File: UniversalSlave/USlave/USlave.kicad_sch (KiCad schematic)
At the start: 18 parts, among them J1 Pluck EADG 1, J2 ISCP, J3 Power In, J4 I2C Test Point, J5 Pluck EADG 2, J6 Mute EADG, J7 I2C Through, J8 I2C In, SW1 SW_Push, U1 PIC16F1788

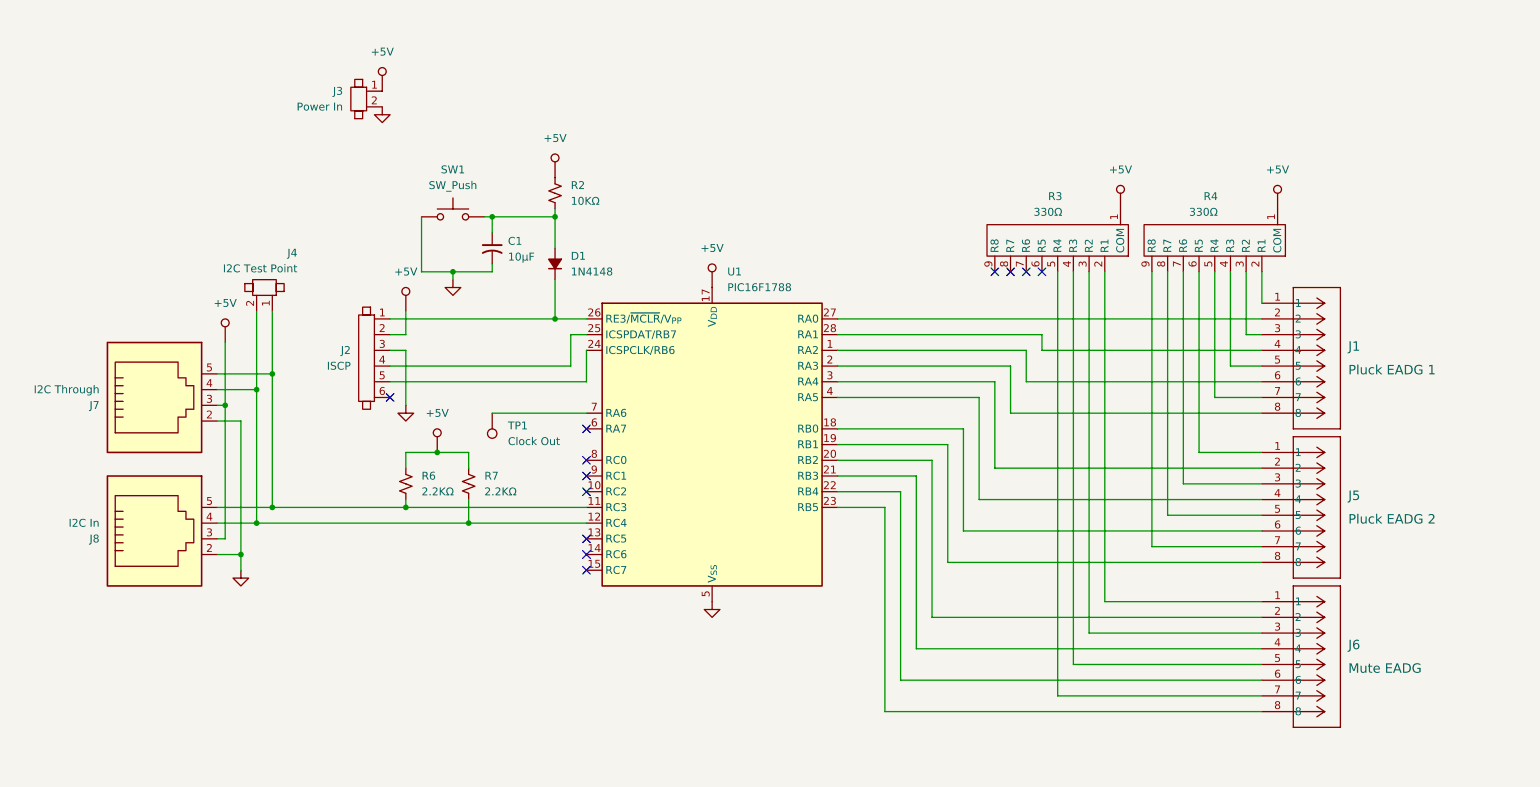
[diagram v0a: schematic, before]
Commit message: decided on utilizing a universal setup for the slave board
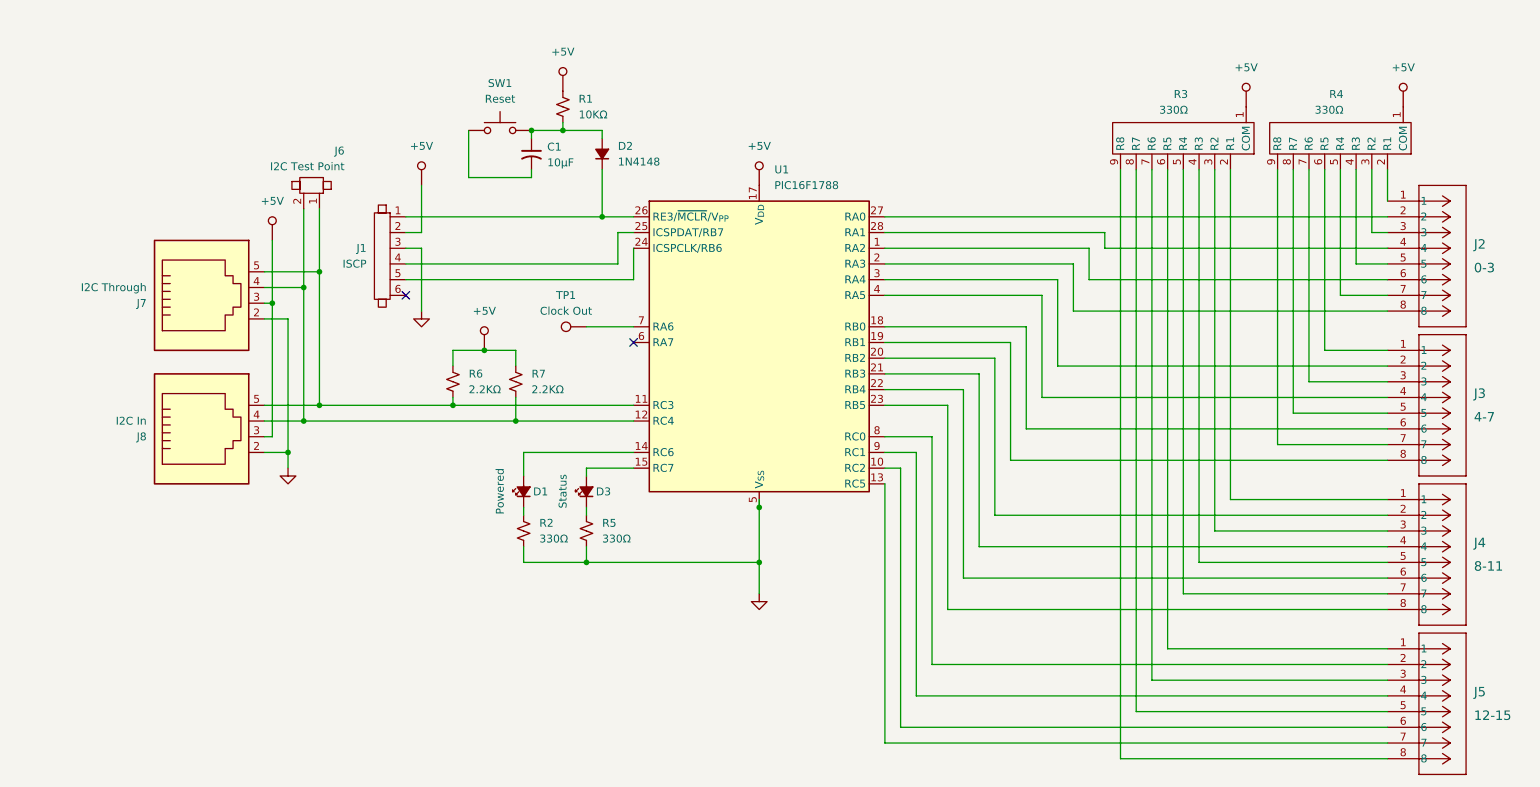
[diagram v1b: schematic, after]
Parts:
- removed D1: 1N4148, symbol Device:D_Small_Filled
- removed J1: Pluck EADG 1, CONN_SD-43045-004_08_MOL, symbol 2_JB_Custom_sym:8PinMolexConn
- removed J2: ISCP, symbol 2_JB_Custom_sym:Jumper_6_Pin
- removed J3: Power In, 2JB_Footprints:1X2_100mil_Header, symbol 2_JB_Custom_sym:Jumper_2_Pin
- removed J4: I2C Test Point, 2JB_Footprints:1X2_100mil_Header, symbol 2_JB_Custom_sym:Jumper_2_Pin
- removed J6: Mute EADG, CONN_SD-43045-004_08_MOL, symbol 2_JB_Custom_sym:8PinMolexConn
- added D1: Powered, symbol Device:LED_Small_Filled
- added D2: 1N4148, symbol Device:D_Small_Filled
- added D3: Status, symbol Device:LED_Small_Filled
- added J1: ISCP, symbol 2_JB_Custom_sym:Jumper_6_Pin
- added J2: 0-3, CONN_SD-43045-004_08_MOL, symbol 2_JB_Custom_sym:8PinMolexConn
- added J3: 4-7, CONN_SD-43045-004_08_MOL, symbol 2_JB_Custom_sym:8PinMolexConn
- added J4: 8-11, CONN_SD-43045-004_08_MOL, symbol 2_JB_Custom_sym:8PinMolexConn
- added J6: I2C Test Point, 2JB_Footprints:1X2_100mil_Header, symbol 2_JB_Custom_sym:Jumper_2_Pin
- added R1: 10KΩ, symbol Device:R_Small_US
- added R5: 330Ω, symbol Device:R_Small_US
- J5: value Pluck EADG 2 -> 12-15
- R2: value 10KΩ -> 330Ω
- SW1: value SW_Push -> Reset
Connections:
- net GND: now also R2.2, J1.3, R5.2; no longer C1.2, SW1.1
- net at C1.1, SW1.2: now also D2.2 (A), R1.2; no longer R2.2
- net at R4.6 (R5): now also J3.1; no longer J5.1
- net at J5.2: now also U1.8 (RC0); no longer U1.3 (RA4)
- net at R4.7 (R6): now also J3.3; no longer J5.3
- net at J5.4: now also U1.9 (RC1); no longer U1.4 (RA5)
- net at R4.8 (R7): now also J3.5; no longer J5.5
- net at J5.6: now also U1.10 (RC2); no longer U1.18 (RB0)
- net at R4.9 (R8): now also J3.7; no longer J5.7
- net at J5.8: now also R3.9 (R8); no longer U1.19 (RB1)
- net at J7.4, J8.4, R7.2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: now also J6.2
- net at J7.5, J8.5, R6.2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: now also J6.1
- net at R4.2 (R1): now also J2.1
- net at U1.27 (RA0): now also J2.2
- net at R4.3 (R2): now also J2.3
- net at U1.28 (RA1): now also J2.4
- net at R4.4 (R3): now also J2.5
- net at U1.1 (RA2): now also J2.6
- net at R4.5 (R4): now also J2.7
- net at U1.2 (RA3): now also J2.8
- net at U1.26 (RE3/~{MCLR}/V_{PP}): now also D2.1 (K), J1.1
- net at U1.25 (ICSPDAT/RB7): now also J1.4
- net at U1.24 (ICSPCLK/RB6): now also J1.5
- net at R2.1: now also D1.1 (K)
- net at R3.2 (R1): now also J4.1
- net at R3.3 (R2): now also J4.3
- net at R3.4 (R3): now also J4.5
- net at R3.5 (R4): now also J4.7
- net at R3.6 (R5): now also J5.1
- net at R3.7 (R6): now also J5.3
- net at R3.8 (R7): now also J5.5
- net at U1.13 (RC5): now also J5.7
- net at U1.14 (RC6): now also D1.2 (A)
- net at U1.15 (RC7): now also D3.2 (A)
- net at U1.20 (RB2): now also J4.2
- net at U1.21 (RB3): now also J4.4
- net at U1.22 (RB4): now also J4.6
- net at U1.23 (RB5): now also J4.8
- new net: D3.1 (K), R5.1
- new net: C1.2, SW1.1
- new net: J3.6, U1.18 (RB0)
- new net: J3.8, U1.19 (RB1)
- new net: J3.2, U1.3 (RA4)
- new net: J3.4, U1.4 (RA5)
- no-connect marks 12 -> 2
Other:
- moved on the sheet: J7, J8, R3, R4, R6, R7, U1

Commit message: designed universal PCB
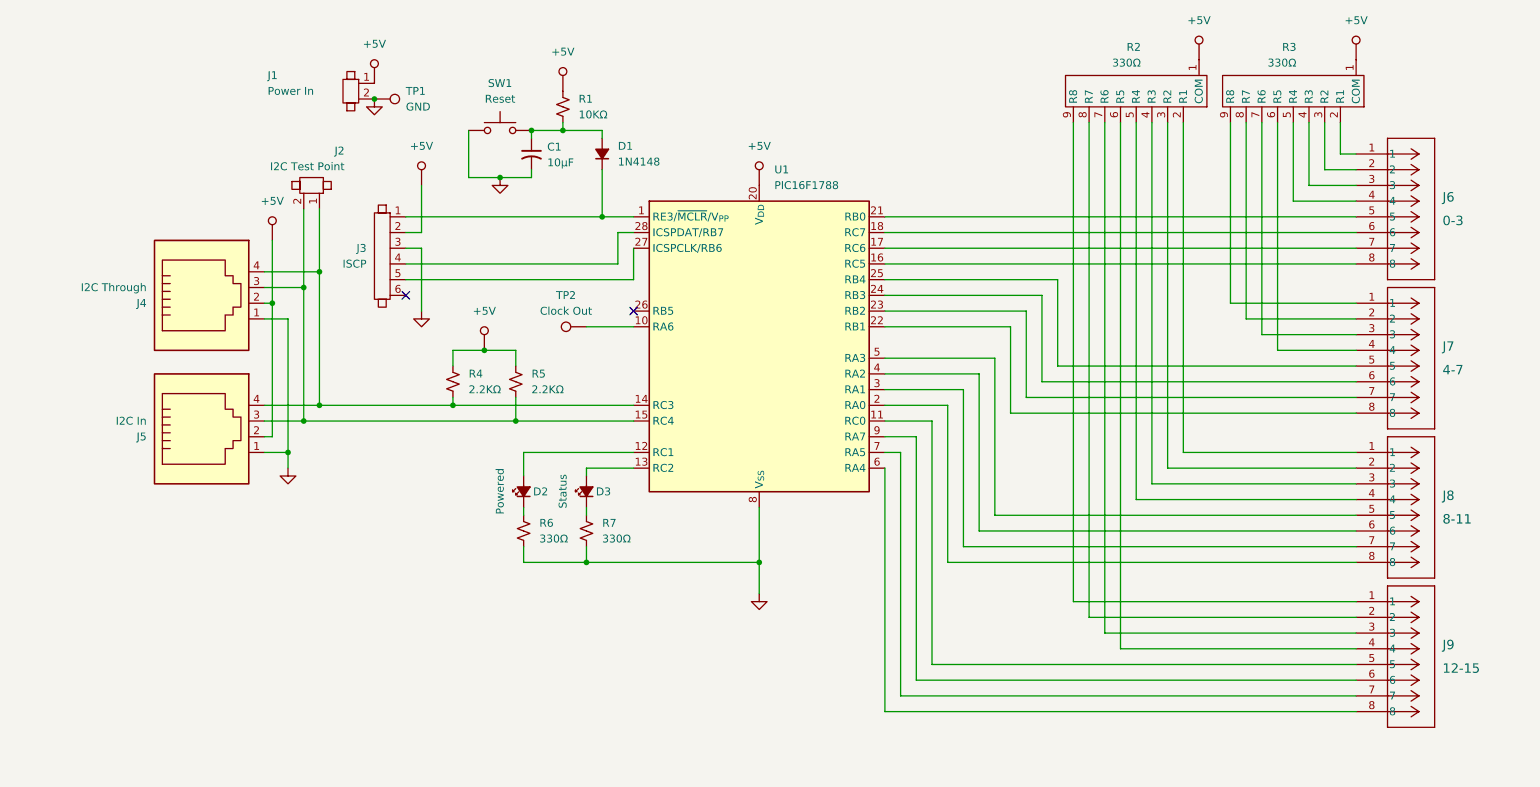
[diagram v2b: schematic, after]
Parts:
- removed J8: I2C In, 2JB_Footprints:RJ11, symbol Connector:RJ11
- added J1: Power In, 2JB_Footprints:2PinMolex, symbol 2_JB_Custom_sym:Jumper_2_Pin
- added J5: I2C In, 2JB_Footprints:RJ11, symbol Connector:RJ11
- added TP1: GND, 2JB_Footprints:1X1_100mil_Header, symbol Connector:TestPoint
- C1: footprint (none) -> Capacitor_THT:C_Radial_D6.3mm_H11.0mm_P2.50mm
- D1: renamed from D2; footprint (none) -> 2JB_Footprints:D_0805
- D2: renamed from D1; footprint (none) -> 2JB_Footprints:D_0805
- D3: footprint (none) -> 2JB_Footprints:D_0805
- J3: renamed from J1; footprint (none) -> 2JB_Footprints:1X6_100mil_Header
- J6: renamed from J2; footprint CONN_SD-43045-004_08_MOL -> 2JB_Footprints:8PinMolex_3.00mmPitch
- J7: renamed from J3; footprint CONN_SD-43045-004_08_MOL -> 2JB_Footprints:8PinMolex_3.00mmPitch
- J8: renamed from J4; footprint CONN_SD-43045-004_08_MOL -> 2JB_Footprints:8PinMolex_3.00mmPitch
- J9: renamed from J5; footprint CONN_SD-43045-004_08_MOL -> 2JB_Footprints:8PinMolex_3.00mmPitch
- R1: footprint (none) -> 2JB_Footprints:C_0805
- R2: renamed from R3; footprint (none) -> 2JB_Footprints:1x9_100mil_Header
- R3: renamed from R4; footprint (none) -> 2JB_Footprints:1x9_100mil_Header
- R6: renamed from R2; footprint (none) -> 2JB_Footprints:C_0805
- R7: renamed from R5; footprint (none) -> 2JB_Footprints:C_0805
- SW1: footprint (none) -> Button_Switch_THT:SW_TH_Tactile_Omron_B3F-100x
- TP2: renamed from TP1; footprint (none) -> 2JB_Footprints:1X1_100mil_Header
- renumbered J6 to J2, J7 to J4, R6 to R4, R7 to R5
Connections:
- net GND: now also C1.2, J4.1, SW1.1, U1.19 (V_{SS}), U1.8 (V_{SS}), J1.2, J5.1, TP1.1; no longer J4.2, U1.16 (V_{SS}), U1.5 (V_{SS})
- net at TP2.1: now also U1.10 (RA6); no longer U1.7 (RA6)
- net at D1.1 (K), J3.1: now also U1.1 (RE3/~{MCLR}/V_{PP}); no longer U1.26 (RE3/~{MCLR}/V_{PP})
- net at J4.3: now also J2.2, R5.2, U1.15 (RC4), J5.3
- net at J2.1, R4.2: now also J4.4, U1.14 (RC3), J5.4; no longer J4.5, U1.11 (RC3)
- net at R3.3 (R2): now also J6.2; no longer J6.3
- net at R3.4 (R3): now also J6.3; no longer J6.5
- net at R3.5 (R4): now also J6.4; no longer J6.7
- net at R3.6 (R5): now also J7.4; no longer J7.1
- net at R3.8 (R7): now also J7.2; no longer J7.5
- net at R3.9 (R8): now also J7.1; no longer J7.7
- net at J9.1: now also R2.9 (R8); no longer R2.6 (R5)
- net at J9.2: now also R2.8 (R7); no longer U1.8 (RC0)
- net at J9.4: now also R2.6 (R5); no longer U1.9 (RC1)
- net at J9.5: now also U1.11 (RC0); no longer R2.8 (R7)
- net at J9.6: now also U1.9 (RA7); no longer U1.10 (RC2)
- net at J9.7: now also U1.7 (RA5); no longer U1.13 (RC5)
- net at J9.8: now also U1.6 (RA4); no longer R2.9 (R8)
- net at J3.4: now also U1.28 (ICSPDAT/RB7); no longer U1.25 (ICSPDAT/RB7)
- net at J3.5: now also U1.27 (ICSPCLK/RB6); no longer U1.24 (ICSPCLK/RB6)
- net at J6.6: now also U1.18 (RC7); no longer U1.1 (RA2)
- net at J6.8: now also U1.16 (RC5); no longer U1.2 (RA3)
- net at D3.2 (A): now also U1.13 (RC2); no longer U1.15 (RC7)
- net at J8.2: now also R2.3 (R2); no longer U1.20 (RB2)
- net at J8.3: now also R2.4 (R3); no longer R2.3 (R2)
- net at U1.21 (RB0): now also J6.5; no longer J8.4
- net at J8.5: now also U1.5 (RA3); no longer R2.4 (R3)
- net at J8.6: now also U1.4 (RA2); no longer U1.22 (RB4)
- net at R2.5 (R4): now also J8.4; no longer J8.7
- net at J8.8: now also U1.2 (RA0); no longer U1.23 (RB5)
- net at D2.2 (A): now also U1.12 (RC1); no longer U1.14 (RC6)
- net at U1.17 (RC6): now also J6.7
- net at J7.6: now also U1.24 (RB3); no longer U1.18 (RB0)
- net at J7.8: now also U1.22 (RB1); no longer U1.19 (RB1)
- net at U1.3 (RA1): now also J8.7; no longer J7.2
- new net: J4.2, J5.2
- new net: J7.7, U1.23 (RB2)
- new net: J7.5, U1.25 (RB4)
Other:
- moved on the sheet: J6, J7, J8, J9, R2, R3
